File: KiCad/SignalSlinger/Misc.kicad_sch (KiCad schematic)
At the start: 14 parts

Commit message: Updated Schematic Rev
Rev 1.2
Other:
- title: SignalSlinger Design -> SignalSlinger
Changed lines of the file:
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@@
   (paper "A4")
   (title_block
-    (title "SignalSlinger Design")
-    (date "2023-07-10")
-    (rev "1.1")
+    (title "SignalSlinger")
+    (date "2023-11-17")
+    (rev "1.2")
   )
   (no_connect (at 208.28 120.65))

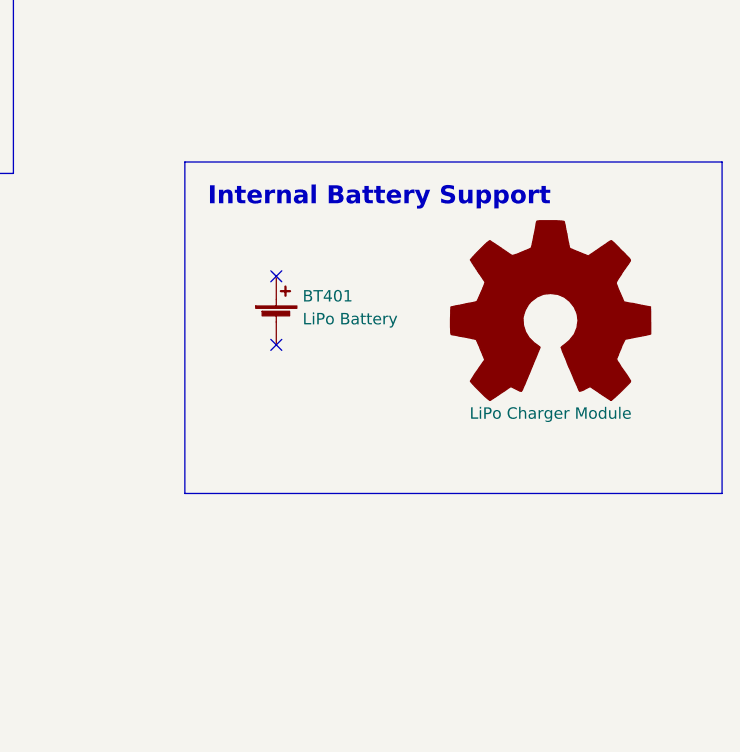
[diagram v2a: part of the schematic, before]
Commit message: DB9 Pinout Updates
o Updated schematic (Rev 2.0)
o Updated PCB
o Updated Gerbers
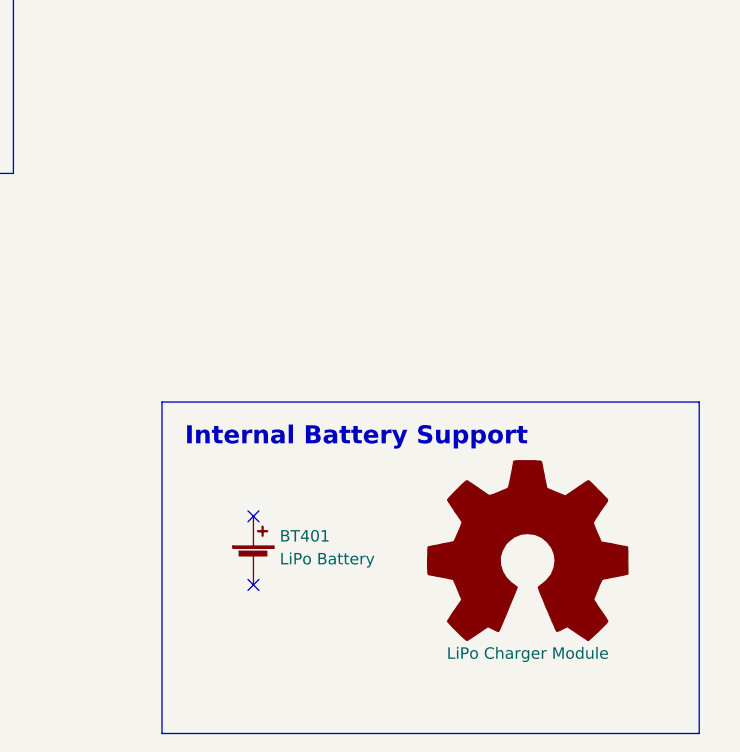
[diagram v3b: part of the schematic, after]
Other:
- moved on the sheet: BT401
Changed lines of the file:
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@@
   (title_block
     (title "SignalSlinger")
-    (date "2023-11-17")
-    (rev "1.2")
-  )
-  (no_connect (at 208.28 120.65))
-  (no_connect (at 208.28 113.03))
+    (date "2023-11-21")
+    (rev "2.0")
+  )
+  (no_connect (at 205.74 147.32))
+  (no_connect (at 205.74 139.7))
   (polyline (pts (xy 48.26 38.1) (xy 48.26 101.6))
     (stroke (width 0) (type default) (color 0 0 0 0))
   )
-  (polyline (pts (xy 257.81 137.16) (xy 198.12 137.16))
+  (polyline (pts (xy 255.27 163.83) (xy 195.58 163.83))
     (stroke (width 0) (type default) (color 0 0 0 0))
   )
@@
     (stroke (width 0) (type default) (color 0 0 0 0))
   )
-  (polyline (pts (xy 257.81 100.33) (xy 257.81 137.16))
+  (polyline (pts (xy 255.27 127) (xy 255.27 163.83))
     (stroke (width 0) (type default) (color 0 0 0 0))
   )
@@
     (stroke (width 0) (type default) (color 0 0 0 0))
   )
-  (polyline (pts (xy 198.12 100.33) (xy 257.81 100.33))
+  (polyline (pts (xy 195.58 127) (xy 255.27 127))
     (stroke (width 0) (type default) (color 0 0 0 0))
   )
@@
     (stroke (width 0) (type default) (color 0 0 0 0))
   )
-  (polyline (pts (xy 198.12 100.33) (xy 198.12 137.16))
+  (polyline (pts (xy 195.58 127) (xy 195.58 163.83))
     (stroke (width 0) (type default) (color 0 0 0 0))
   )
@@
     (effects (font (size 2 2) (thickness 0.4) bold) (justify left bottom))
   )
-  (text "Internal Battery Support" (at 200.66 105.41 0)
+  (text "Internal Battery Support" (at 198.12 132.08 0)
     (effects (font (size 2 2) (thickness 0.4) bold) (justify left bottom))
   )
@@
     )
   )
-  (symbol (lib_id "Device:Battery_Cell") (at 208.28 118.11 0) (unit 1)
-    (in_bom yes) (on_board yes) (fields_autoplaced)
-    (property "Reference" "BT401" (id 0) (at 211.201 115.2433 0)
+  (symbol (lib_id "Device:Battery_Cell") (at 205.74 144.78 0) (unit 1)
+    (in_bom yes) (on_board yes) (fields_autoplaced)
+    (property "Reference" "BT401" (id 0) (at 208.661 141.9133 0)
       (effects (font (size 1.27 1.27)) (justify left))
     )
-    (property "Value" "LiPo Battery" (id 1) (at 211.201 117.7802 0)
+    (property "Value" "LiPo Battery" (id 1) (at 208.661 144.4502 0)
       (effects (font (size 1.27 1.27)) (justify left))
     )
-    (property "Footprint" "" (id 2) (at 208.28 116.586 90)
-      (effects (font (size 1.27 1.27)) hide)
-    )
-    (property "Datasheet" "" (id 3) (at 208.28 116.586 90)
-      (effects (font (size 1.27 1.27)) hide)
-    )
-    (property "Link" "https://www.adafruit.com/product/258" (id 4) (at 208.28 118.11 0)
-      (effects (font (size 1.27 1.27)) hide)
-    )
-    (property "Manufacturer" "Adafruit" (id 5) (at 208.28 118.11 0)
-      (effects (font (size 1.27 1.27)) hide)
-    )
-    (property "Manufacturer PN" "258" (id 6) (at 208.28 118.11 0)
-      (effects (font (size 1.27 1.27)) hide)
-    )
-    (property "Description" "Lithium Ion Polymer Battery - 3.7v 1200mAh" (id 7) (at 208.28 118.11 0)
+    (property "Footprint" "" (id 2) (at 205.74 143.256 90)
+      (effects (font (size 1.27 1.27)) hide)
+    )
+    (property "Datasheet" "" (id 3) (at 205.74 143.256 90)
+      (effects (font (size 1.27 1.27)) hide)
+    )
+    (property "Link" "https://www.adafruit.com/product/258" (id 4) (at 205.74 144.78 0)
+      (effects (font (size 1.27 1.27)) hide)
+    )
+    (property "Manufacturer" "Adafruit" (id 5) (at 205.74 144.78 0)
+      (effects (font (size 1.27 1.27)) hide)
+    )
+    (property "Manufacturer PN" "258" (id 6) (at 205.74 144.78 0)
+      (effects (font (size 1.27 1.27)) hide)
+    )
+    (property "Description" "Lithium Ion Polymer Battery - 3.7v 1200mAh" (id 7) (at 205.74 144.78 0)
       (effects (font (size 1.27 1.27)) hide)
     )
@@
     )
   )
-  (symbol (lib_id "Graphic:Logo_Open_Hardware_Large") (at 238.76 118.11 0) (unit 1)
-    (in_bom yes) (on_board yes) (fields_autoplaced)
-    (property "Reference" "HDWR407" (id 0) (at 238.76 105.41 0)
-      (effects (font (size 1.27 1.27)) hide)
-    )
-    (property "Value" "LiPo Charger Module" (id 1) (at 238.76 128.27 0))
-    (property "Footprint" "" (id 2) (at 238.76 118.11 0)
-      (effects (font (size 1.27 1.27)) hide)
-    )
-    (property "Datasheet" "" (id 3) (at 238.76 118.11 0)
-      (effects (font (size 1.27 1.27)) hide)
-    )
-    (property "Description" "Micro-Lipo Charger for LiPo/LiIon Batt" (id 7) (at 238.76 118.11 0)
-      (effects (font (size 1.27 1.27)) hide)
-    )
-    (property "Digi-Key Part No." "1528-1833-ND" (id 8) (at 238.76 118.11 0)
-      (effects (font (size 1.27 1.27)) hide)
-    )
-    (property "Link" "https://www.digikey.com/en/products/detail/adafruit-industries-llc/1904/5054545" (id 9) (at 238.76 118.11 0)
-      (effects (font (size 1.27 1.27)) hide)
-    )
-    (property "Manufacturer" "Adafruit Industries LLC" (id 10) (at 238.76 118.11 0)
-      (effects (font (size 1.27 1.27)) hide)
-    )
-    (property "Manufacturer PN" "1904" (id 11) (at 238.76 118.11 0)
-      (effects (font (size 1.27 1.27)) hide)
-    )
+  (symbol (lib_id "Graphic:Logo_Open_Hardware_Large") (at 236.22 144.78 0) (unit 1)
+    (in_bom yes) (on_board yes) (fields_autoplaced)
+    (property "Reference" "HDWR407" (id 0) (at 236.22 132.08 0)
+      (effects (font (size 1.27 1.27)) hide)
+    )
+    (property "Value" "LiPo Charger Module" (id 1) (at 236.22 154.94 0))
+    (property "Footprint" "" (id 2) (at 236.22 144.78 0)
+      (effects (font (size 1.27 1.27)) hide)
+    )
+    (property "Datasheet" "" (id 3) (at 236.22 144.78 0)
+      (effects (font (size 1.27 1.27)) hide)
+    )
+    (property "Description" "Micro-Lipo Charger for LiPo/LiIon Batt" (id 7) (at 236.22 144.78 0)
+      (effects (font (size 1.27 1.27)) hide)
+    )
+    (property "Digi-Key Part No." "1528-1833-ND" (id 8) (at 236.22 144.78 0)
+      (effects (font (size 1.27 1.27)) hide)
+    )
+    (property "Link" "https://www.digikey.com/en/products/detail/adafruit-industries-llc/1904/5054545" (id 9) (at 236.22 144.78 0)
+      (effects (font (size 1.27 1.27)) hide)
+    )
+    (property "Manufacturer" "Adafruit Industries LLC" (id 10) (at 236.22 144.78 0)
+      (effects (font (size 1.27 1.27)) hide)
+    )
+    (property "Manufacturer PN" "1904" (id 11) (at 236.22 144.78 0)
+      (effects (font (size 1.27 1.27)) hide)
+    )
